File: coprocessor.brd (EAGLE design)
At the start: 27.9 x 48.1 mm, 15 parts, among them IC1 MEGA32U2, Y1 16MHZ

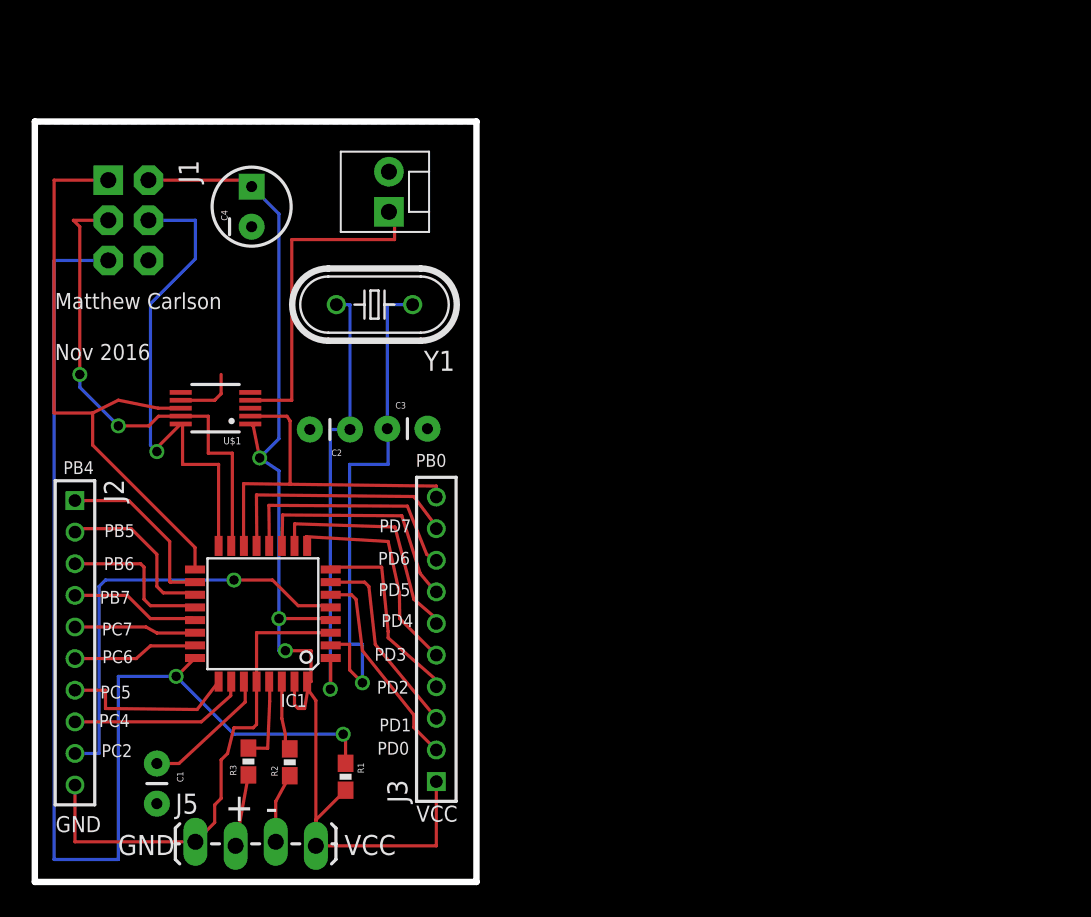
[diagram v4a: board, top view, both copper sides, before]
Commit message: added the custom library and power controller
started to integrate the custom power controller to the coprocessor
board so it can be powered by the battery. I  need to figure out how to
enable the raspberry pi
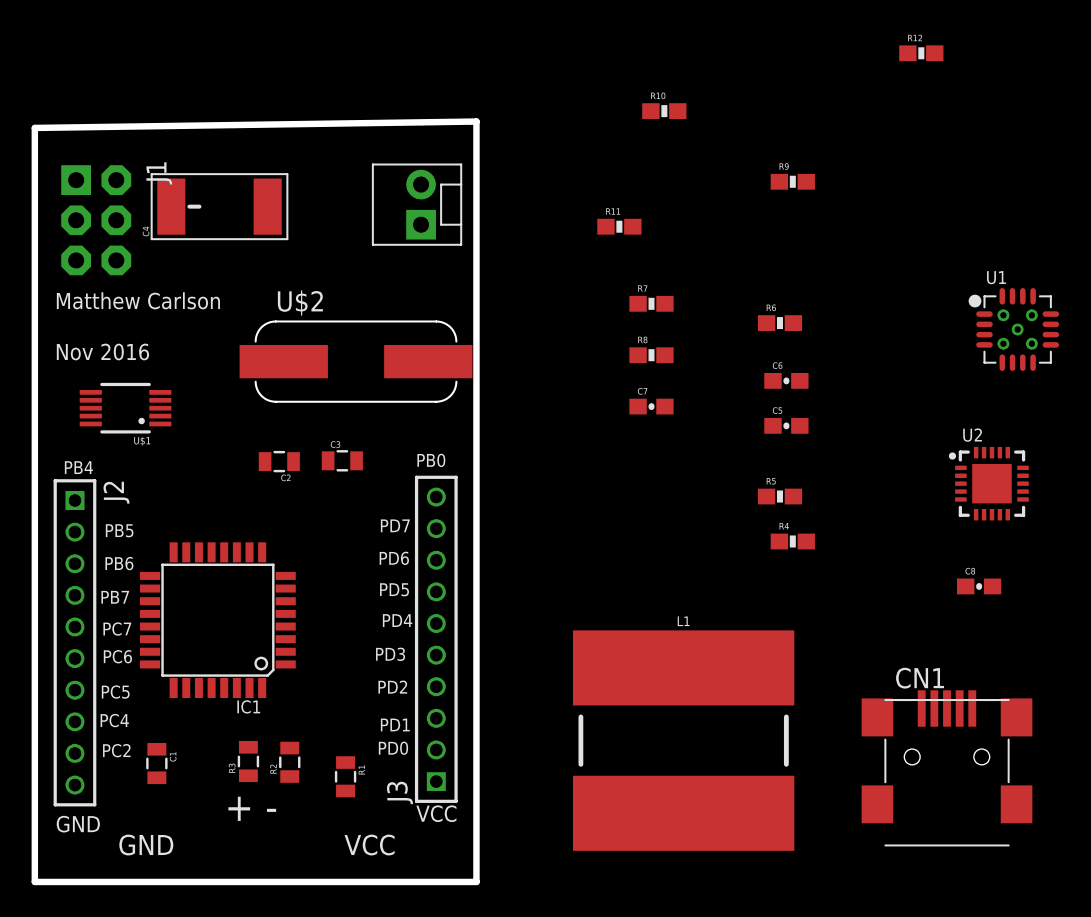
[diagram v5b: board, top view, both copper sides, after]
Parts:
- removed J5: (no value), SparkFun-Connectors:1X04_LOCK_LONGPADS
- removed Y1: 16MHZ, SparkFun-FreqCtrl:HC49U-V
- added C5: 0.1uF, SparkFun-Capacitors:0603-CAP
- added C6: 1.0uF, SparkFun-Capacitors:0603-CAP
- added C7: 2.2uF, SparkFun-Capacitors:0603-CAP
- added C8: 10uF, SparkFun-Capacitors:0603-CAP
- added CN1: (no value), adafruit:USB-MINIB
- added FRAME2: FRAME-LETTERNO_PACKAGE, SparkFun-Aesthetics:DUMMY
- added L1: 6.8uH, SparkFun-Coils:INDUCTOR_SDR1307
- added R10, R12: 100k, SparkFun-Resistors:0603-RES
- added R11: 1K, SparkFun-Resistors:0603-RES
- added R4: 340, SparkFun-Resistors:0603-RES
- added R5, R7: 1.86m, SparkFun-Resistors:0603-RES
- added R6, R8: 200k, SparkFun-Resistors:0603-RES
- added R9: 270k, SparkFun-Resistors:0603-RES
- added U$2: 16MHZ, custom:HC49/US
- added U1: (no value), custom:MICROBUILDER_PVQFN-16
- added U2: (no value), custom:MICROBUILDER_QFN20_4MM
- C1, C2, C3: device SparkFun-Capacitors:CAP-PTH-SMALL -> SparkFun-Capacitors:0805
- C4: device SparkFun-Capacitors:CPOL-RADIAL-10UF-25V -> SparkFun-Capacitors:VISHAY_C
- R1, R2, R3: device SparkFun-Resistors:0603-RES -> SparkFun-Resistors:0805
- moved U$1 5.69 mm to (5.74, 30.0)
- moved C2 4.91 mm to (15.5, 26.6)
- moved C3 3.50 mm to (19.5, 26.6)
- moved IC1 2.87 mm to (11.6, 16.6)
- moved J4 2.19 mm to (24.4, 41.6)
- moved C4 2.03 mm to (11.7, 42.7)
- moved J1 2.03 mm to (3.89, 41.9)
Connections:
- new net 5V: C7.1, R7.2, U1.1, U1.15, U1.16
- new net DATA+: CN1.D+, R2.1
- new net DATA-: CN1.D-, R3.1
- new net N$11: L1.P$2, U1.3, U1.4
- new net N$12: R11.2, U2.P$13
- new net N$13: R7.1, R8.2, U1.14
- new net N$14: R12.2, U2.P$12
- new net N$6: R4.2, R5.1, U1.9
- new net V_BATT: C5.1, C6.1, L1.P$1, R5.2, R6.2, U1.8, U2.P$1, U2.P$20
- new net V_USB: C8.1, CN1.VBUS, R9.2, U2.P$17, U2.P$18, U2.P$19, U2.P$3, U2.P$4, U2.P$9
- net GND: now also C4.-, C5.2, C6.2, C7.2, C8.2, CN1.GND, R10.1, R11.1, R12.1, R4.1, R8.1, U1.10, U1.13, U1.5, U1.6, U1.7, U1.P$18, U1.P$19, U1.P$20, U1.P$21, U1.P$22, U2.P$10, U2.P$11, U2.P$21; no longer C4.2, J5.1
- net N$1: now also R10.2, R9.1, U2.P$2; no longer J5.2, R3.1
- net N$10: now also U$2.P$1; no longer Y1.1
- net N$4: now also R6.1, U1.11; no longer J5.3, R2.1
- net N$9: now also U$2.P$2; no longer Y1.2
- net VCC: now also C4.+; no longer C4.1, J5.4
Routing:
- net VCC: track 77.9 -> 0.00 mm, vias 3 -> 0
- net RESET: track 76.3 -> 0.00 mm, vias 2 -> 0
- net MISO: track 39.0 -> 0.00 mm
- net GND: track 35.3 -> 0.00 mm
- net N$10: track 32.9 -> 0.00 mm, vias 1 -> 0
- net SCK: track 32.1 -> 0.00 mm, vias 2 -> 0
- net MOSI: track 31.4 -> 0.00 mm, vias 1 -> 0
- net N$9: track 28.4 -> 0.00 mm, vias 1 -> 0
- net PC2: track 27.6 -> 0.00 mm, vias 1 -> 0
- net PB0: track 23.5 -> 0.00 mm
- net DAC_VOUT: track 21.4 -> 0.00 mm
- net PD7: track 15.7 -> 0.00 mm
- net PD6: track 15.4 -> 0.00 mm
- net PD5: track 15.0 -> 0.00 mm
- net PD4: track 14.7 -> 0.00 mm
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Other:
- outline, holes or cut-outs redrawn

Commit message: finished the power
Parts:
- added B1: (no value), custom:MICROBUILDER_JSTPH2
- added C10: (no value), SparkFun-Capacitors:EIA3216
- added C9: 10uF, SparkFun-Capacitors:0603-CAP
- added D2: (no value), custom:MICROBUILDER_CHIPLED_0603
- added LOGO1: OSHW-LOGOS, SparkFun-Aesthetics:OSHW-LOGO-S
- added R13: 1K, SparkFun-Resistors:0603-RES
- added T1: (no value), custom:TRANSISTOR_SC59-BEC
- moved R8 7.33 mm to (32.1, 35.8)
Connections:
- new net N$15: T1.B, U1.12
- new net N$16: R13.2, T1.C
- new net N$17: D2.A, R13.1
- new net N$8: B1.2, C9.1, U2.P$14, U2.P$15, U2.P$16
- net 5V: now also C10.A
- net GND: now also B1.1, C10.C, C9.2, D2.C
- net V_BATT: now also T1.E

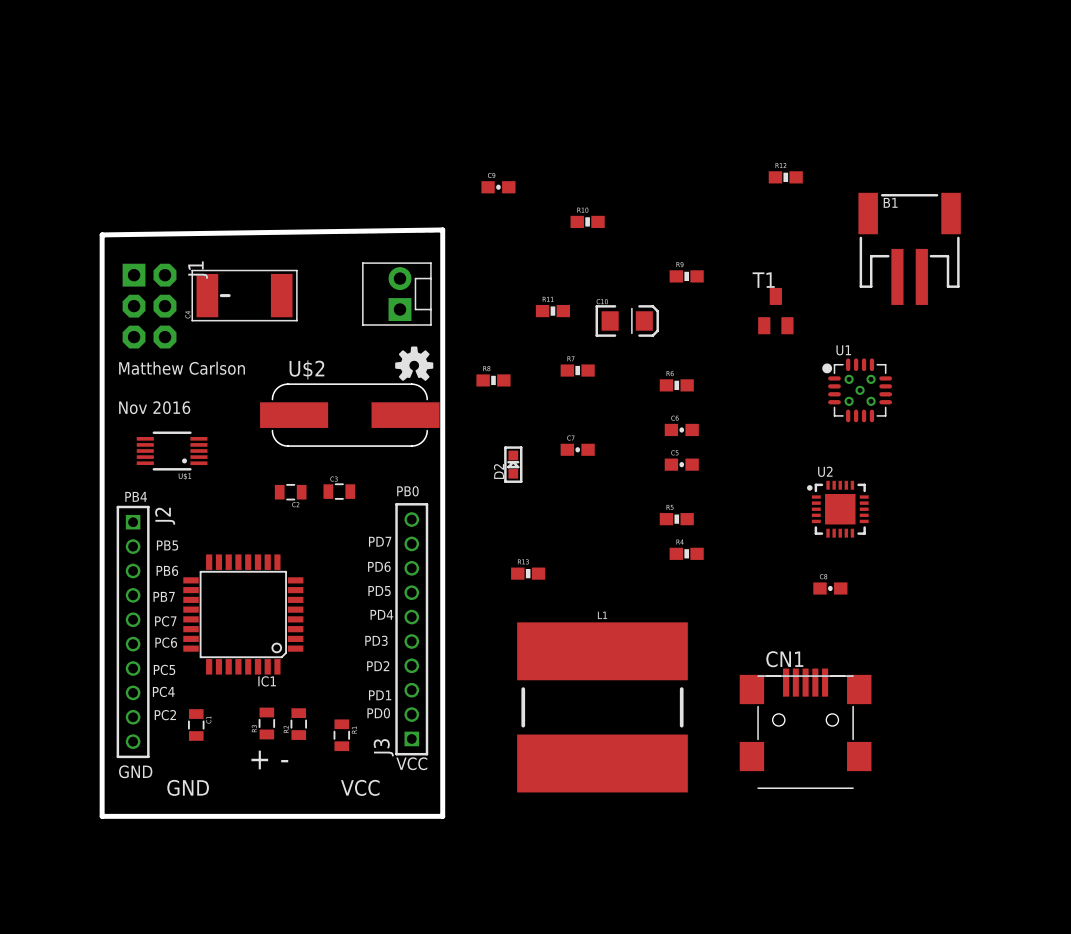
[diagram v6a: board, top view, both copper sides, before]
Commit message: Added a few parts to the custom lib and added more to the coprocessor
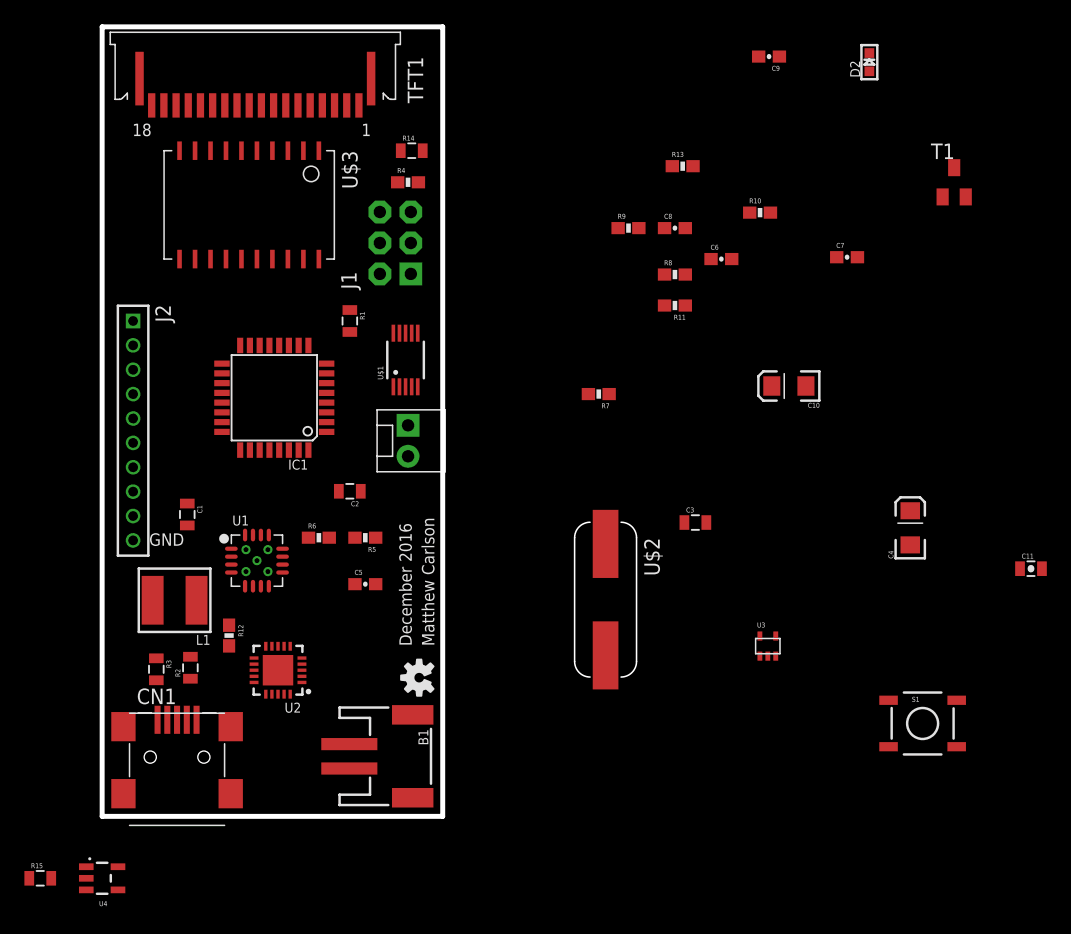
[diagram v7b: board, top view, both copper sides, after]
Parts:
- removed FRAME2: FRAME-LETTERNO_PACKAGE, SparkFun-Aesthetics:DUMMY
- removed J3: (no value), SparkFun-Connectors:1X10-2MM
- added C11: 10uF, SparkFun-Capacitors:0805-CAP
- added R14: 5k, SparkFun-Resistors:0805
- added R15: 3.9, SparkFun-Resistors:0805
- added S1: RESET, SparkFun-Electromechanical:TACTILE-SWITCH-SMD
- added TFT1: TFT-18-1.0MM, custom:TFT-CONN-18
- added U$3: CBT3244AD, custom:S020-75MM
- added U3: V_REG_LDOSMD2, SparkFun-PowerIC:SC70
- added U4: AZV321, custom:SOT23-5
- C4: device SparkFun-Capacitors:VISHAY_C -> SparkFun-Capacitors:EIA3216
- L1: device SparkFun-Coils:INDUCTOR_SDR1307 -> custom:MICROBUILDER_INDUCTOR_5X5MM_NR5040_NOTHERMALS
- moved B1 60.3 mm to (24.0, 4.93), turned to 270 degrees
- moved R12 59.2 mm to (10.4, 14.8), turned to 270 degrees
- moved C4 57.8 mm to (66.3, 23.7)
- moved CN1 51.7 mm to (6.15, 3.86)
- moved U1 51.4 mm to (12.7, 21.0)
- moved U2 48.0 mm to (14.4, 12.0), turned to 180 degrees
- moved D2 44.1 mm to (62.9, 61.9)
- moved R4 38.1 mm to (25.1, 52.0)
- moved L1 36.2 mm to (5.94, 17.7), turned to 180 degrees
- moved R13 35.7 mm to (47.6, 53.3)
- moved R1 34.0 mm to (20.3, 40.6)
- moved C8 32.2 mm to (47.0, 48.3)
- moved R6 31.9 mm to (17.8, 22.9)
- moved C3 29.3 mm to (48.7, 24.1)
- moved C5 27.7 mm to (21.6, 19.1)
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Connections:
- removed net PC2: IC1.5, J2.9
- removed net PC4: IC1.26, J2.8
- removed net PD2: IC1.8, J3.4
- removed net PD4: IC1.10, J3.6
- new net 2.8V: C11.1, TFT1.9, U3.5
- new net N$18: J2.8
- new net N$19: R15.2, TFT1.10
- new net N$20: R15.1, U4.3, U4.4
- new net N$24: U$3.P$12
- new net N$25: U$3.P$4
- new net N$26: U$3.P$6
- new net N$27: U$3.P$8
- new net N$5: U$3.P$2
- new net PB2: R14.1, U$3.P$1
- new net TFT_CS: TFT1.5
- new net TFT_LED: U4.1
- new net TFT_RESET: TFT1.2
- new net TFT_RS: TFT1.4
- net GND: now also C11.2, C4.C, S1.1, TFT1.1, TFT1.11, TFT1.12, TFT1.13, TFT1.14, TFT1.8, U$3.P$10, U3.2, U4.2; no longer C4.-
- net MISO: now also TFT1.7, U$3.P$18
- net MOSI: now also TFT1.6, U$3.P$14
- net PB0: no longer J3.10
- net PD0: no longer J3.2
- net PD1: no longer J3.3
- net PD3: no longer J3.5
- net PD5: no longer J3.7
- net PD6: no longer J3.8
- net PD7: no longer J3.9
- net RESET: now also S1.3
- net SCK: now also TFT1.3, U$3.P$16
- net VCC: now also C4.A, J2.9, R14.2, U$3.P$20, U3.1, U3.3, U4.5; no longer C4.+, J3.1
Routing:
- added copper zone on layer 16, net GND
- removed copper zone on layer 16, net N$5
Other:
- board size 27.9 x 48.1 mm -> 27.9 x 64.8 mm
- board text added: "December 2016"
- board text removed: "+"
- board text removed: "-"
- board text removed: "Nov 2016"
- board text removed: "PB0"
- board text removed: "PB4"
- board text removed: "PB5"
- board text removed: "PB6"
- board text removed: "PB7"
- board text removed: "PC2"
- board text removed: "PC4"
- board text removed: "PC5"
- board text removed: "PC6"
- board text removed: "PC7"
- board text removed: "PD0"
- board text removed: "PD1"
- board text removed: "PD2"
- board text removed: "PD3"
- board text removed: "PD4"
- board text removed: "PD5"
- board text removed: "PD6"
- board text removed: "PD7"
- board text removed: "VCC"

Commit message: Added a cool logo
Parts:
- added FRAME2: FRAME-LETTER, SparkFun-Aesthetics:CREATIVE_COMMONS
- added LED1: DONE, adafruit:CHIPLED_0603
- added LED2: CHG, adafruit:CHIPLED_0603
- added R16, R17: 1K, SparkFun-Resistors:0603-RES
- added THERM: 16k, SparkFun-Resistors:0603-RES
- added U$4: (no value), custom:LOGO_1INCH
- C10: value (none) -> 100uF
- R4: value 340 -> 340k
- R5, R7: value 1.86m -> 1.87M
- U1: value (none) -> TPS61090RSAR
- moved R15 74.5 mm to (31.8, 59.7)
- moved U4 70.8 mm to (38.1, 54.6)
- moved C6 43.3 mm to (7.62, 48.3), flipped to the bottom, turned to 180 degrees
- moved LOGO1 27.4 mm to (52.7, 5.03)
- moved U$3 6.35 mm to (17.8, 57.1), flipped to the bottom, turned to 90 degrees
- flipped C11 to the bottom
- flipped C3 to the bottom
- flipped C7 to the bottom
- flipped C8 to the bottom
- flipped R10 to the bottom
- flipped R11 to the bottom
- flipped R13 to the bottom
- flipped R7 to the bottom
- flipped R8 to the bottom
- flipped R9 to the bottom
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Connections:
- removed net PB4: IC1.18, J2.1
- removed net PB5: IC1.19, J2.2
- removed net PB6: IC1.20, J2.3
- removed net PB7: IC1.21, J2.4
- removed net PC5: IC1.25, J2.7
- removed net PC6: IC1.23, J2.6
- removed net PC7: IC1.22, J2.5
- removed net PD1: IC1.7
- removed net PD3: IC1.9
- new net N$21: R17.1, U2.P$8
- new net N$22: LED1.C, R16.2
- new net N$23: LED2.C, R17.2
- net GND: now also THERM.1; no longer J2.10
- net MISO: no longer U$3.P$18
- net N$18: now also R16.1, U2.P$7; no longer J2.8
- net N$24: now also THERM.2, U2.P$5; no longer U$3.P$12
- net TFT_CS: now also IC1.9, U$3.P$18
- net TFT_LED: now also IC1.7
- net TFT_RS: now also IC1.8, U$3.P$12
- net VCC: no longer J2.9
- net V_USB: now also LED1.A, LED2.A
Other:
- board text added: "Coprocessor demo"
